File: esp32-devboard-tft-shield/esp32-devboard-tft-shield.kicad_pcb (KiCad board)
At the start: 2 copper layers, 40.6 x 59.7 mm, 5 parts, among them J1 11x10, J1 Conn_02x20, J2 Conn_01x40, J3 Conn_01x12

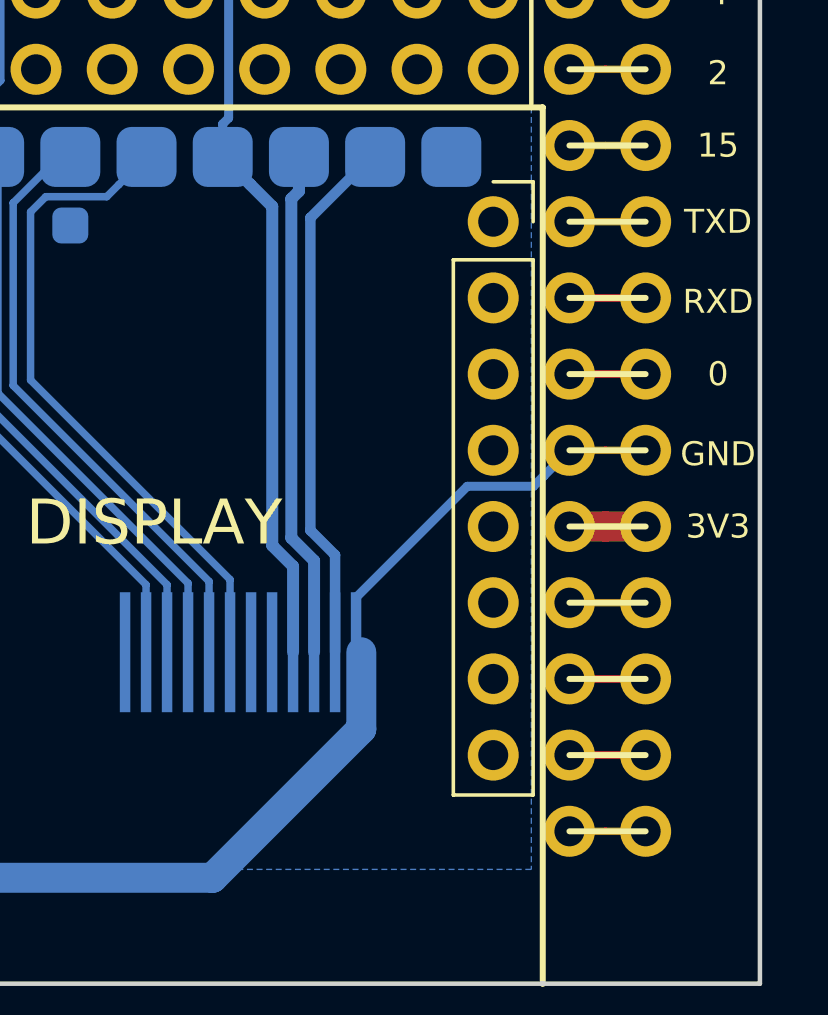
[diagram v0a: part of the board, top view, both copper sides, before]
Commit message: fix socket location
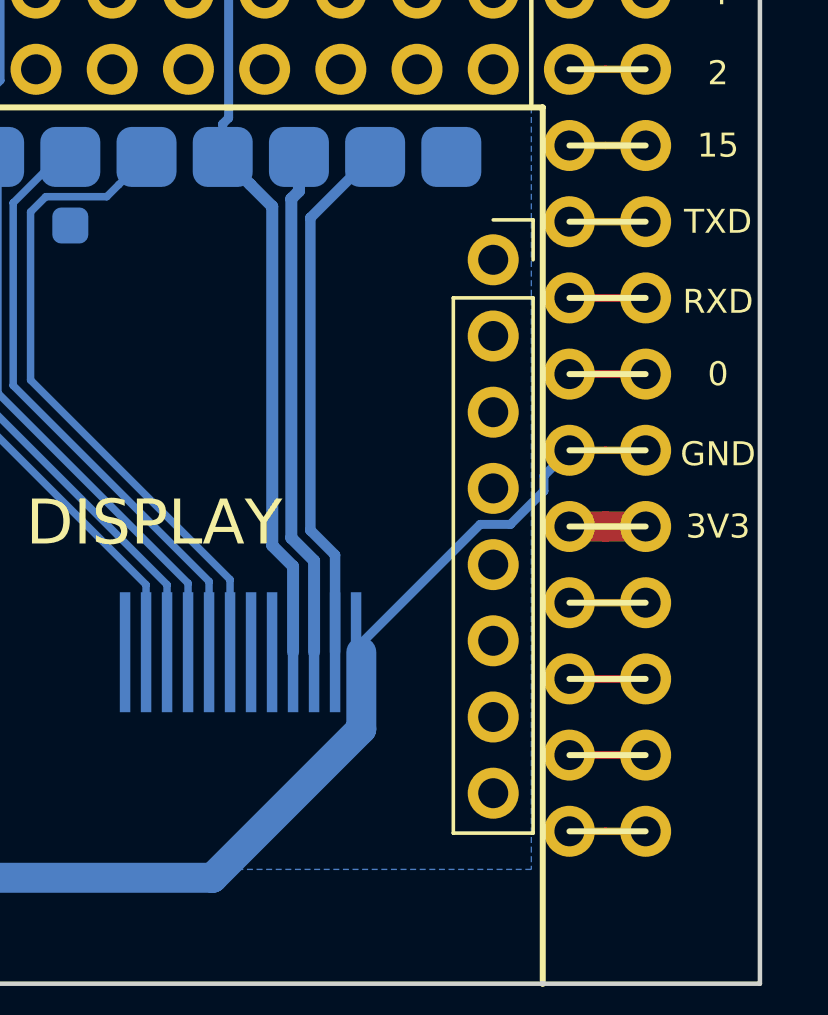
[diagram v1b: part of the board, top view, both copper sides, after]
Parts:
- moved REF** 1.27 mm to (162.6, 113.0)
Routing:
- net GND: track 97.0 -> 96.2 mm

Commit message: tft shield update
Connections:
- J2 pad 29: GND -> Net-(J2-Pad29)
- J2 pad 30: GND -> Net-(J2-Pad29)
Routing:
- net GND: track 96.2 -> 83.8 mm
- net Net-(J2-Pad29): track 0.00 -> 2.54 mm
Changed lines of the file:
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@@
     (thickness 1.6)
     (drawings 117)
-    (tracks 155)
+    (tracks 150)
     (zones 0)
     (modules 5)
-    (nets 45)
+    (nets 46)
   )
   (page A4)
@@
   (net 43 /RXD)
   (net 44 /0)
+  (net 45 "Net-(J2-Pad29)")
   (net_class Default "これはデフォルトのネット クラスです。"
     (clearance 0.2)
@@
     (add_net "Net-(J1-Pad37)")
     (add_net "Net-(J1-Pad39)")
+    (add_net "Net-(J2-Pad29)")
     (add_net "Net-(J2-Pad31)")
     (add_net "Net-(J2-Pad33)")
@@
       (net 44 /0))
     (pad 29 thru_hole oval (at 0 -35.56 180) (size 1.7 1.7) (drill 1) (layers *.Cu *.Mask)
-      (net 5 GND))
+      (net 45 "Net-(J2-Pad29)"))
     (pad 30 thru_hole oval (at 2.54 -35.56 180) (size 1.7 1.7) (drill 1) (layers *.Cu *.Mask)
-      (net 5 GND))
+      (net 45 "Net-(J2-Pad29)"))
     (pad 31 thru_hole oval (at 0 -38.1 180) (size 1.7 1.7) (drill 1) (layers *.Cu *.Mask)
       (net 21 "Net-(J2-Pad31)"))
@@
   (segment (start 134.62 83.82) (end 137.16 83.82) (width 1) (layer F.Cu) (net 5))
   (segment (start 133.875999 133.630001) (end 153.204001 133.630001) (width 1) (layer B.Cu) (net 5))
+  (segment (start 158.163001 126.111) (end 158.163001 125.810997) (width 0.3) (layer B.Cu) (net 5))
+  (segment (start 153.204001 133.630001) (end 158.163001 128.671001) (width 1) (layer B.Cu) (net 5))
+  (segment (start 158.163001 128.671001) (end 158.163001 126.111) (width 1) (layer B.Cu) (net 5))
+  (segment (start 134.62 83.82) (end 131.58501 86.85499) (width 1) (layer B.Cu) (net 5))
+  (segment (start 131.58501 86.85499) (end 131.58501 131.339012) (width 1) (layer B.Cu) (net 5))
   (segment (start 131.58501 131.339012) (end 133.875999 133.630001) (width 1) (layer B.Cu) (net 5))
-  (segment (start 131.58501 86.85499) (end 131.58501 131.339012) (width 1) (layer B.Cu) (net 5))
-  (segment (start 134.62 83.82) (end 131.58501 86.85499) (width 1) (layer B.Cu) (net 5))
-  (segment (start 166.302081 119.38) (end 167.64 119.38) (width 0.25) (layer F.Cu) (net 5))
-  (segment (start 165.1 119.38) (end 166.302081 119.38) (width 0.25) (layer F.Cu) (net 5))
-  (segment (start 158.163001 128.671001) (end 158.163001 126.111) (width 1) (layer B.Cu) (net 5))
-  (segment (start 153.204001 133.630001) (end 158.163001 128.671001) (width 1) (layer B.Cu) (net 5))
-  (segment (start 164.250001 120.229999) (end 165.1 119.38) (width 0.3) (layer B.Cu) (net 5))
-  (segment (start 164.250001 120.736001) (end 164.250001 120.229999) (width 0.3) (layer B.Cu) (net 5))
-  (segment (start 163.136001 121.850001) (end 164.250001 120.736001) (width 0.3) (layer B.Cu) (net 5))
-  (segment (start 162.123997 121.850001) (end 163.136001 121.850001) (width 0.3) (layer B.Cu) (net 5))
-  (segment (start 158.163001 125.810997) (end 162.123997 121.850001) (width 0.3) (layer B.Cu) (net 5))
-  (segment (start 158.163001 126.111) (end 158.163001 125.810997) (width 0.3) (layer B.Cu) (net 5))
+  (segment (start 166.302081 119.38) (end 167.64 119.38) (width 1) (layer F.Cu) (net 45) (status 1000000))
+  (segment (start 165.1 119.38) (end 166.302081 119.38) (width 1) (layer F.Cu) (net 45) (status 1000000))
   (segment (start 166.302081 83.82) (end 167.64 83.82) (width 0.25) (layer F.Cu) (net 6))
   (segment (start 165.1 83.82) (end 166.302081 83.82) (width 0.25) (layer F.Cu) (net 6))
